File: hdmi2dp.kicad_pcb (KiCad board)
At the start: 2 copper layers, 48.2 x 54.1 mm, 28 parts, among them J1 HDMI_A, J2 47272-0001, U1 AMS1117-3.3

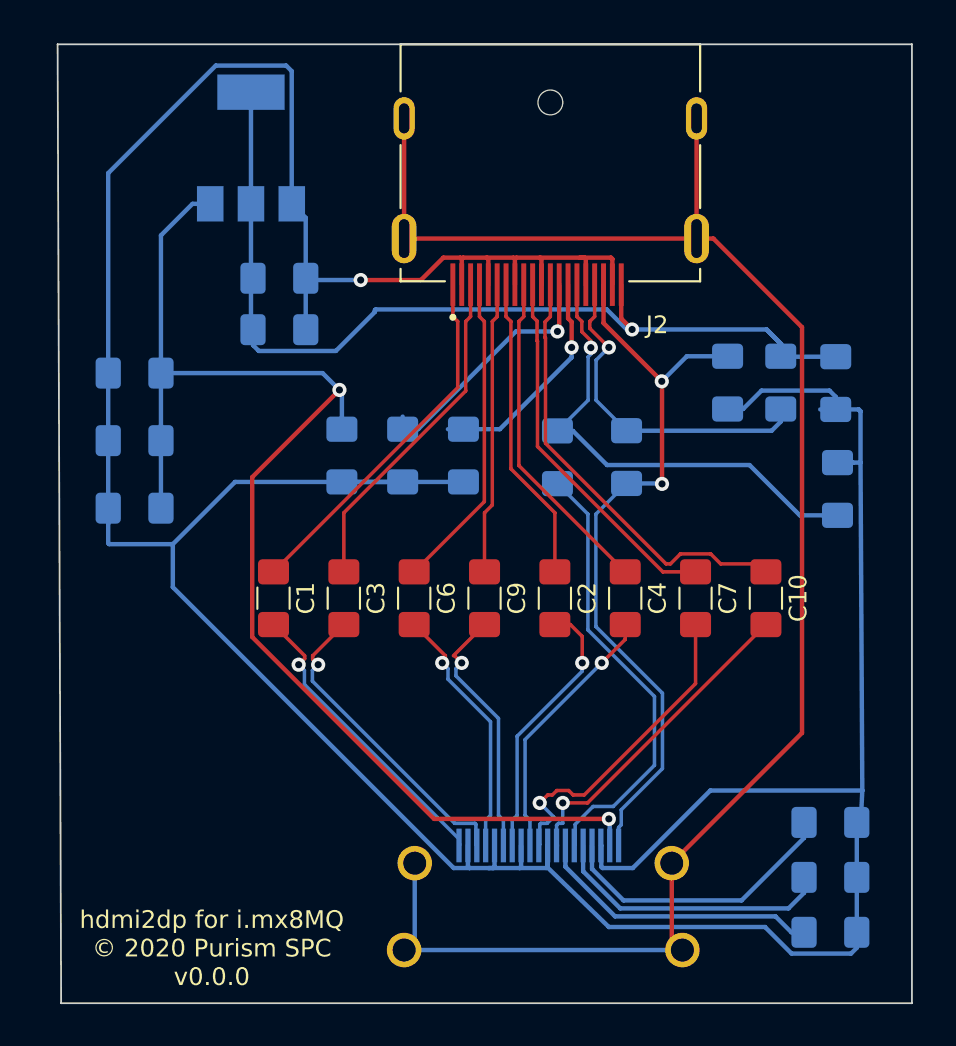
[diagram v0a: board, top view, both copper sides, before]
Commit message: Reroute the diff pairs based on the impedance calculations using Beta Layout's stackup
Also made the board 4 layers, fixed up the silkscreen, and added 3d models for the receptacles.
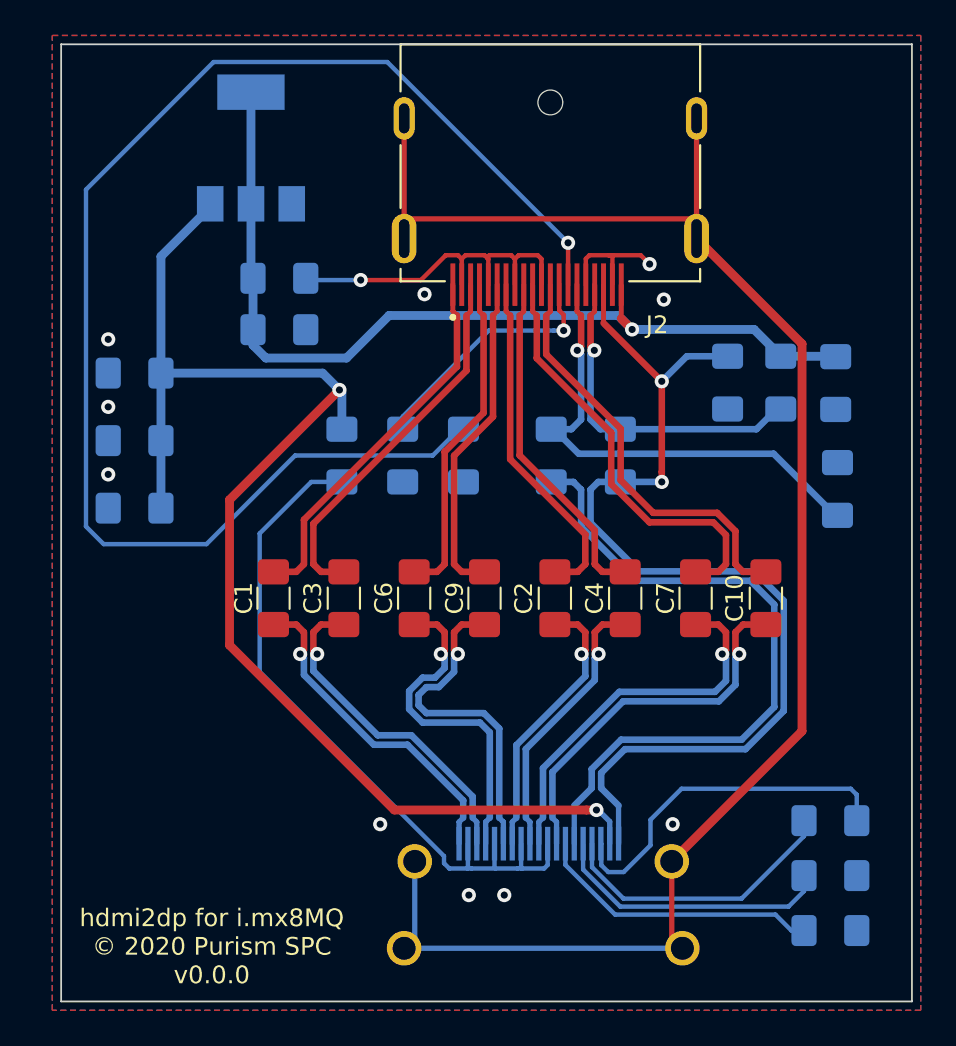
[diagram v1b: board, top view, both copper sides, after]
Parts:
- moved C15 0.36 mm to (109.7, 87.2)
- moved C16 0.36 mm to (113.5, 87.2)
- moved J1 0.10 mm to (109.2, 110.1)
- moved R8 0.10 mm to (125.4, 107.8)
- moved R3 0.10 mm to (125.4, 114.0)
- moved R7 0.10 mm to (125.4, 110.9)
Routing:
- net GND: track 218.4 -> 88.1 mm, vias 1 -> 11
- net Net-(J2-Pad14): track 12.8 -> 80.2 mm
- net /HDMI_HEACN: track 43.1 -> 58.2 mm
- net /HDMI_HEACP: track 25.2 -> 38.8 mm
- net /HDMI_TX1P: track 14.5 -> 19.1 mm
- net /HDMI_TX1N: track 14.6 -> 19.1 mm
- net /DP3_P: track 21.1 -> 24.3 mm
- net /HDMI_CLKN: track 18.4 -> 21.5 mm
- net /HDMI_CLKP: track 18.4 -> 21.5 mm
- net /DP1_N: track 16.5 -> 18.7 mm
- net /DP0_N: track 19.2 -> 21.3 mm
- net /DP2_P: track 17.3 -> 19.5 mm
- net /VDD_3V3: track 54.4 -> 52.5 mm
- net /HDMI_TX2P: track 17.2 -> 18.9 mm
- net Earth: track 97.4 -> 98.9 mm
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- added copper zone on B.Cu, net GND
- added copper zone on F.Cu, net GND
- added copper zone on In1.Cu, net GND
- added copper zone on In2.Cu, net GND
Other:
- board size 48.2 x 54.1 mm -> 48 x 54 mm
- copper layers 2 -> 4
- net class 100Ohm_Diff_Pair added: clearance 0.159999, trace_width 0.373179, via_dia 0.8, via_drill 0.4

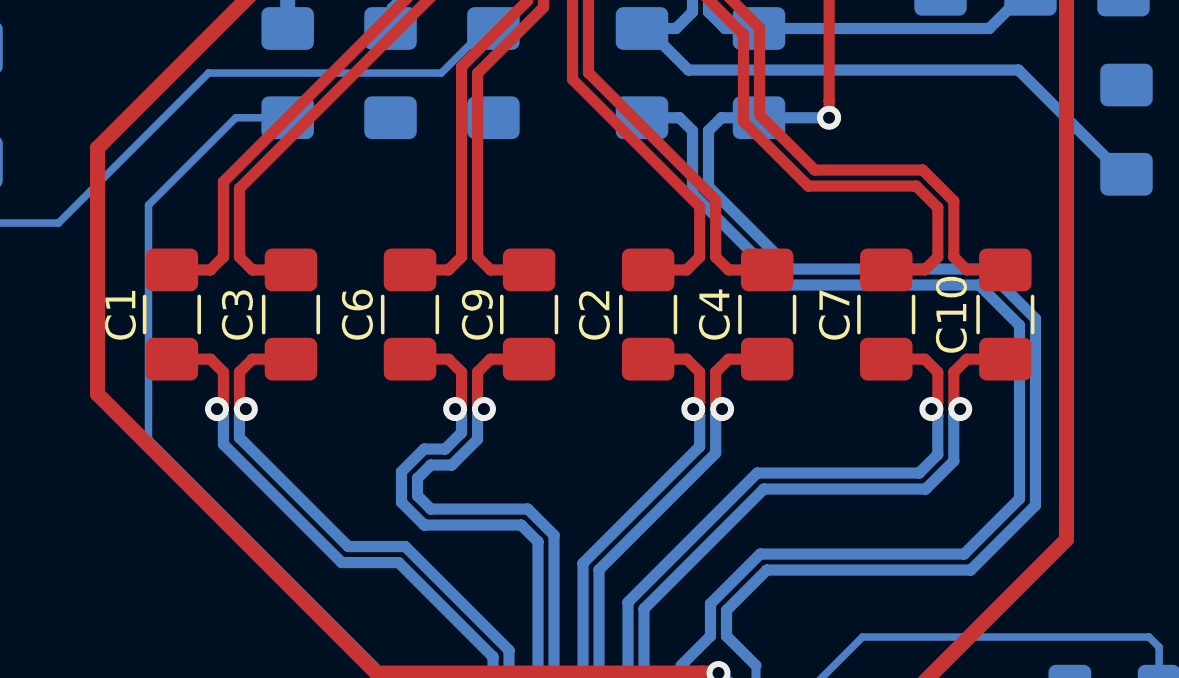
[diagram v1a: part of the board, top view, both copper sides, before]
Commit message: Add HDMI and DP lane pair names to silk screen
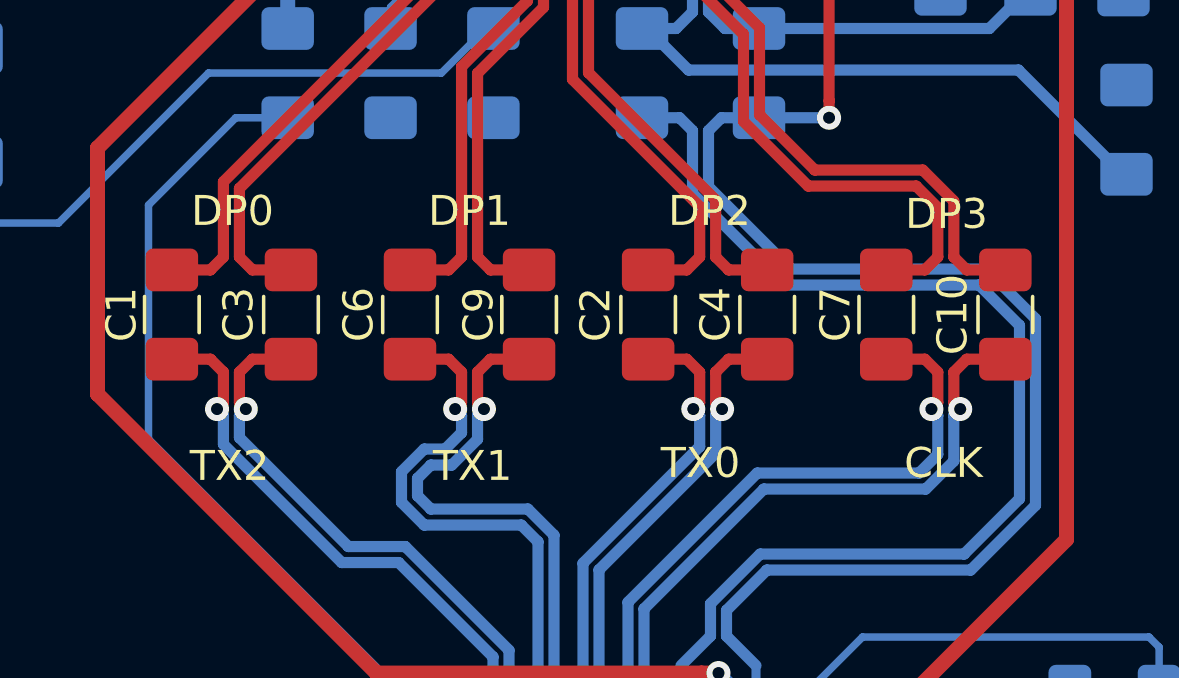
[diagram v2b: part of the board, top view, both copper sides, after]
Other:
- board text added: "CLK"
- board text added: "DP0"
- board text added: "DP1"
- board text added: "DP2"
- board text added: "DP3"
- board text added: "DP_AUX"
- board text added: "TX0"
- board text added: "TX1"
- board text added: "TX2"
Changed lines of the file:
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@@
-(kicad_pcb (version 20171130) (host pcbnew 5.1.5-1.fc31)
+(kicad_pcb (version 20171130) (host pcbnew 5.1.5+dfsg1-2+b1)
   (general
     (thickness 1.6)
-    (drawings 9)
+    (drawings 18)
     (tracks 395)
     (zones 0)
@@
     )
   )
+  (gr_text DP_AUX (at 111.7 83.5) (layer B.SilkS)
+    (effects (font (size 1 1) (thickness 0.15)) (justify mirror))
+  )
+  (gr_text DP3 (at 119.8 91.9) (layer F.SilkS)
+    (effects (font (size 1 1) (thickness 0.15)))
+  )
+  (gr_text DP2 (at 111.9 91.8) (layer F.SilkS)
+    (effects (font (size 1 1) (thickness 0.15)))
+  )
+  (gr_text DP1 (at 103.9 91.8) (layer F.SilkS)
+    (effects (font (size 1 1) (thickness 0.15)))
+  )
+  (gr_text DP0 (at 96 91.8) (layer F.SilkS)
+    (effects (font (size 1 1) (thickness 0.15)))
+  )
+  (gr_text TX2 (at 95.9 100.3) (layer F.SilkS)
+    (effects (font (size 1 1) (thickness 0.15)))
+  )
+  (gr_text CLK (at 119.7 100.2) (layer F.SilkS)
+    (effects (font (size 1 1) (thickness 0.15)))
+  )
+  (gr_text TX0 (at 111.6 100.2) (layer F.SilkS)
+    (effects (font (size 1 1) (thickness 0.15)))
+  )
+  (gr_text TX1 (at 104 100.3) (layer F.SilkS)
+    (effects (font (size 1 1) (thickness 0.15)))
+  )
   (dimension 48 (width 0.15) (layer Cmts.User)
